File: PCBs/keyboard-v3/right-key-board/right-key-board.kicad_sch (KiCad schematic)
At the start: 0 parts

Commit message: Key board schematic done and layout half done
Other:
- added sheet Keys (keys.kicad_sch)
- added sheet MCU (mcu.kicad_sch)

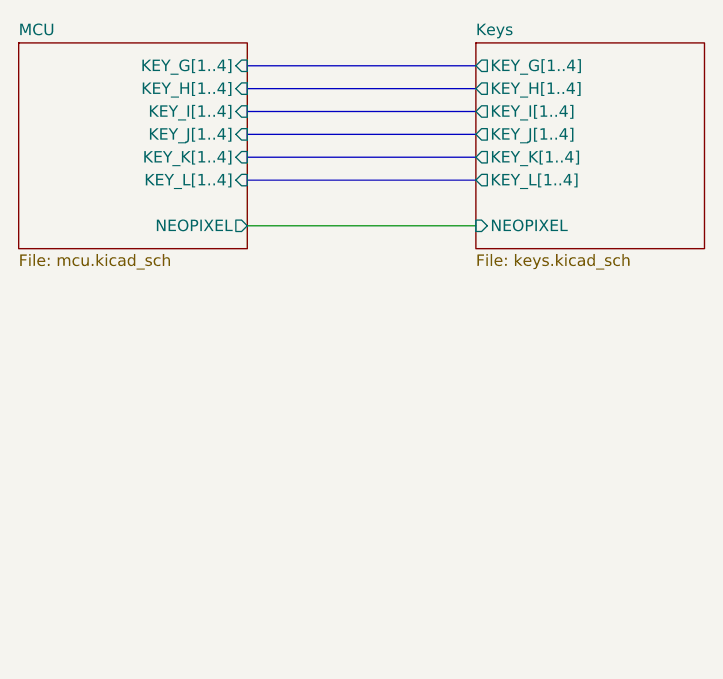
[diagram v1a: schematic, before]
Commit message: Added mounting holes
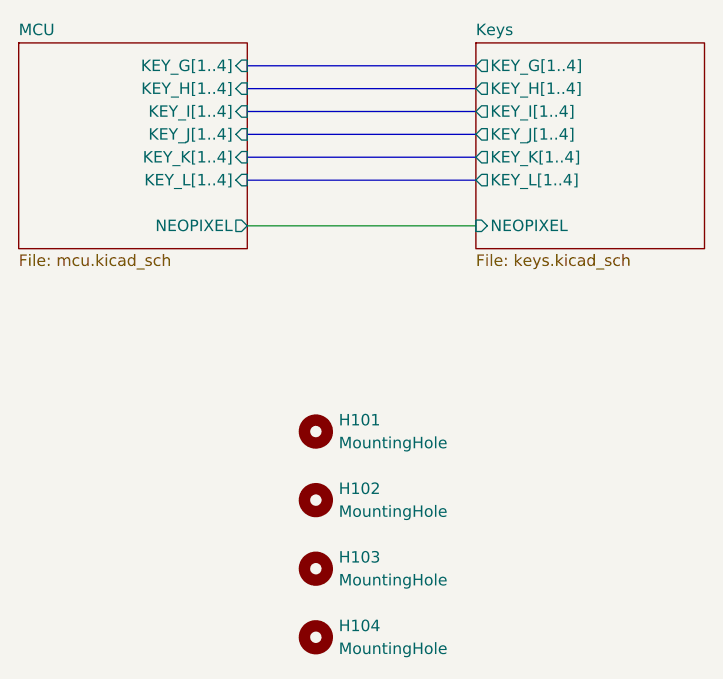
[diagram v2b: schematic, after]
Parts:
- added H101, H102, H103, H104: MountingHole, MountingHole:MountingHole_2.2mm_M2, symbol Mechanical:MountingHole
